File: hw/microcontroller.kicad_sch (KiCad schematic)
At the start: 65 parts, among them J201 68710814022, J202 FTSH-105-01-L-DV-K, SW201 Push button switch, U201 STM32H753VITx, U202 USB3343, Y201 26MHz, Y202 26MHz

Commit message: Now two CPLDs, new placement for better routing of clocks and symmetry for delay. Not routed yet but placement is "complete".
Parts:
- R221, R223, R224: footprint Resistor_SMD:R_0603_1608Metric -> Resistor_SMD:R_0402_1005Metric
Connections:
- net atten.12dB: now reaches U201.55 (PD8)
- net atten.6dB: now reaches U201.56 (PD9)
- net atten.3dB: now reaches U201.57 (PD10)
- net cpld1.NSS: now reaches U201.77 (PA15)
- net filter.BPFMid: now reaches U201.81 (PD0)
- net filter.BPFMid2: now reaches U201.82 (PD1)
- net filter.BPFHi: now reaches U201.83 (PD2)
- net filter.BPFLo1: now reaches U201.84 (PD3)
- net filter.HPF: now reaches U201.85 (PD4)
- net filter.BPFLo2: now reaches U201.86 (PD5)
- net atten.24dB: now reaches U201.88 (PD7)
- net cpld.MISO renamed cpld0.MISO
- net cpld.MOSI renamed cpld0.MOSI
- net cpld.NSS renamed cpld0.NSS
- net cpld.SCK renamed cpld0.SCK
- no-connect marks 37 -> 26
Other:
- note added: "SPI1=n/u SPI2=disp SPI3=cpld0/1 SPI4=osd0/1 SPI5=n/u SPI6=n/u"
- note removed: "SPI1=n/u SPI2=disp SPI3=cpld SPI4=osd0/1 SPI5=n/u SPI6=n/u"

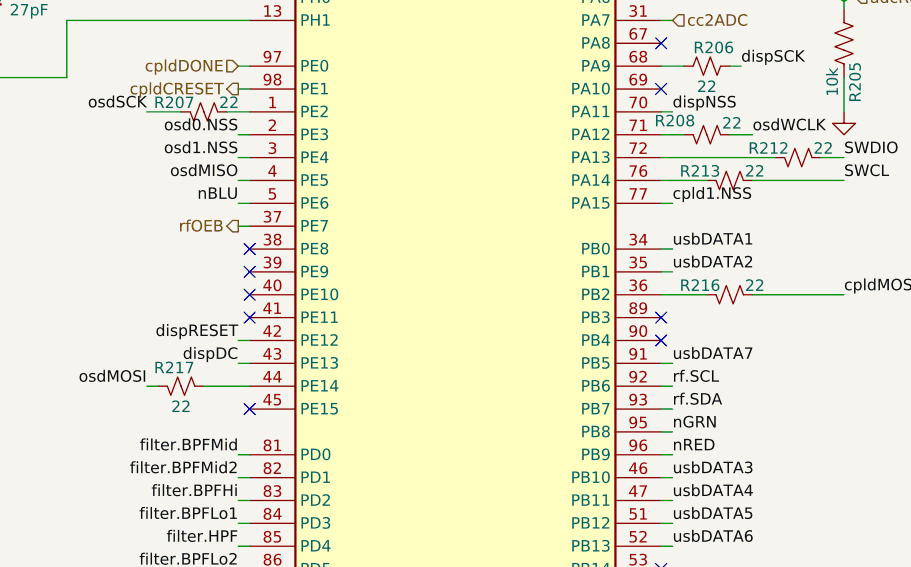
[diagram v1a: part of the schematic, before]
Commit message: PCB and schematic both pass DRC and all nets routed. Now for some desk checking...
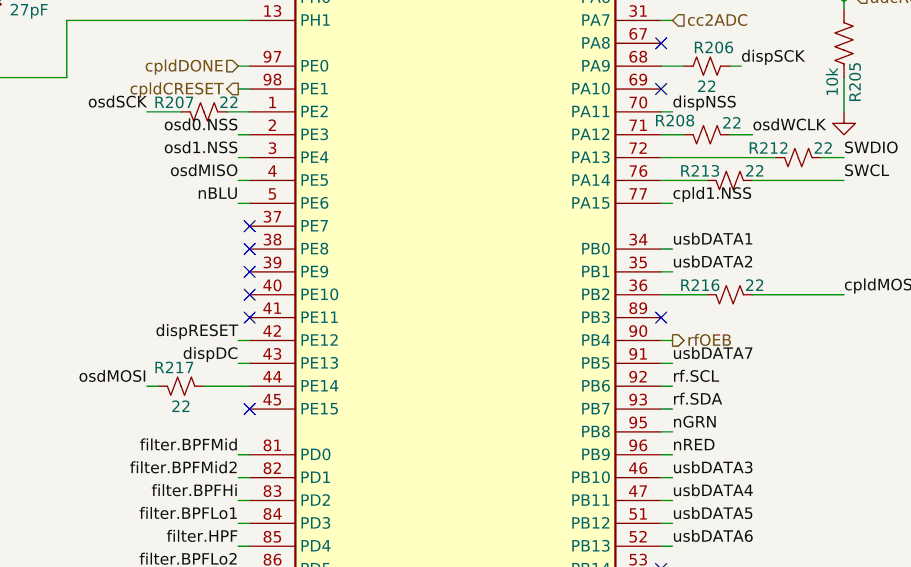
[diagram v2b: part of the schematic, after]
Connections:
- net rfOEB: now also U201.90 (PB4); no longer U201.37 (PE7)
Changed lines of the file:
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@@
 	)
 	(no_connect
-		(at 102.87 87.63)
-	)
-	(no_connect
 		(at 102.87 59.69)
 	)
@@
 	)
 	(no_connect
+		(at 57.15 74.93)
+	)
+	(no_connect
 		(at 102.87 151.13)
 	)
@@
 	(wire
 		(pts
-			(xy 55.88 74.93) (xy 57.15 74.93)
-		)
-		(stroke
-			(width 0)
-			(type default)
-		)
-	)
-	(wire
-		(pts
 			(xy 161.29 97.79) (xy 161.29 99.06)
 		)
@@
 	(wire
 		(pts
+			(xy 104.14 87.63) (xy 102.87 87.63)
+		)
+		(stroke
+			(width 0)
+			(type default)
+		)
+	)
+	(wire
+		(pts
 			(xy 134.62 133.35) (xy 134.62 134.62)
 		)
@@
 		)
 	)
+	(hierarchical_label "rfOEB"
+		(shape output)
+		(at 104.14 87.63 0)
+		(effects
+			(font
+				(size 1.27 1.27)
+			)
+			(justify left)
+		)
+	)
 	(hierarchical_label "rf{I2C}"
 		(shape bidirectional)
@@
 		)
 	)
-	(hierarchical_label "rfOEB"
-		(shape output)
-		(at 55.88 74.93 180)
-		(effects
-			(font
-				(size 1.27 1.27)
-			)
-			(justify right)
-		)
-	)

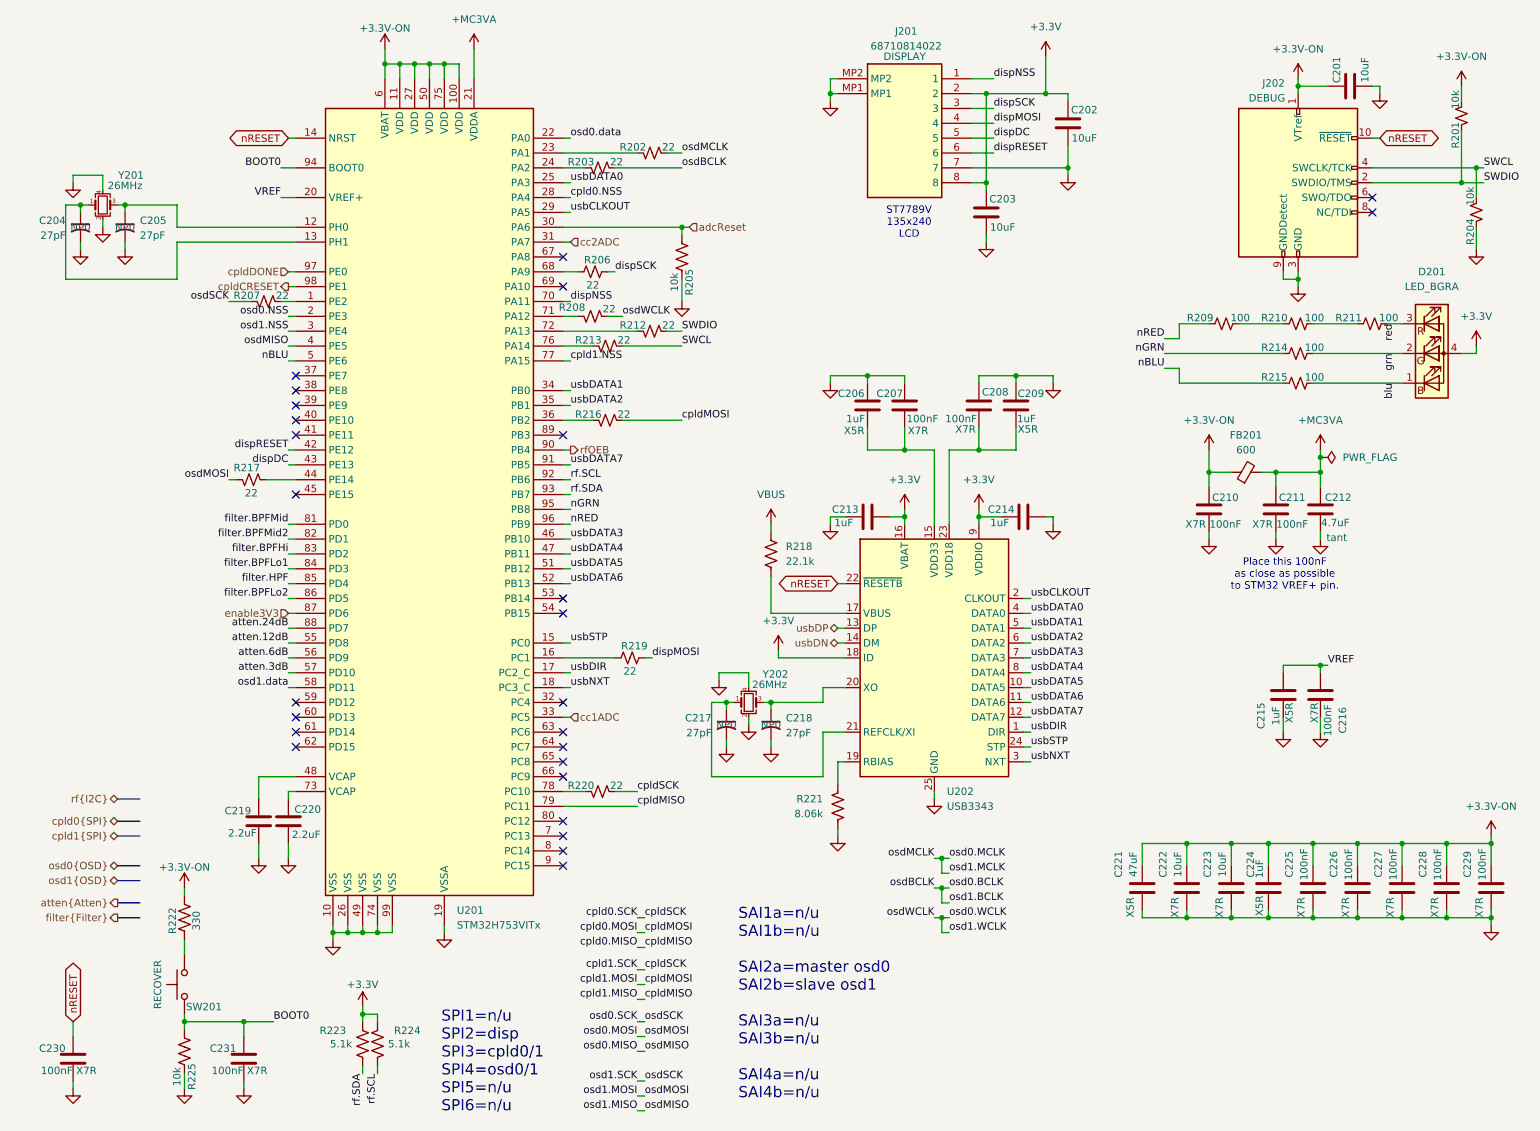
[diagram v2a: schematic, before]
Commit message: 3D rendering now. All DRCs pass on schematic and PCB. BOM scrubbed to coallesce parts. Still no part numbers for most.
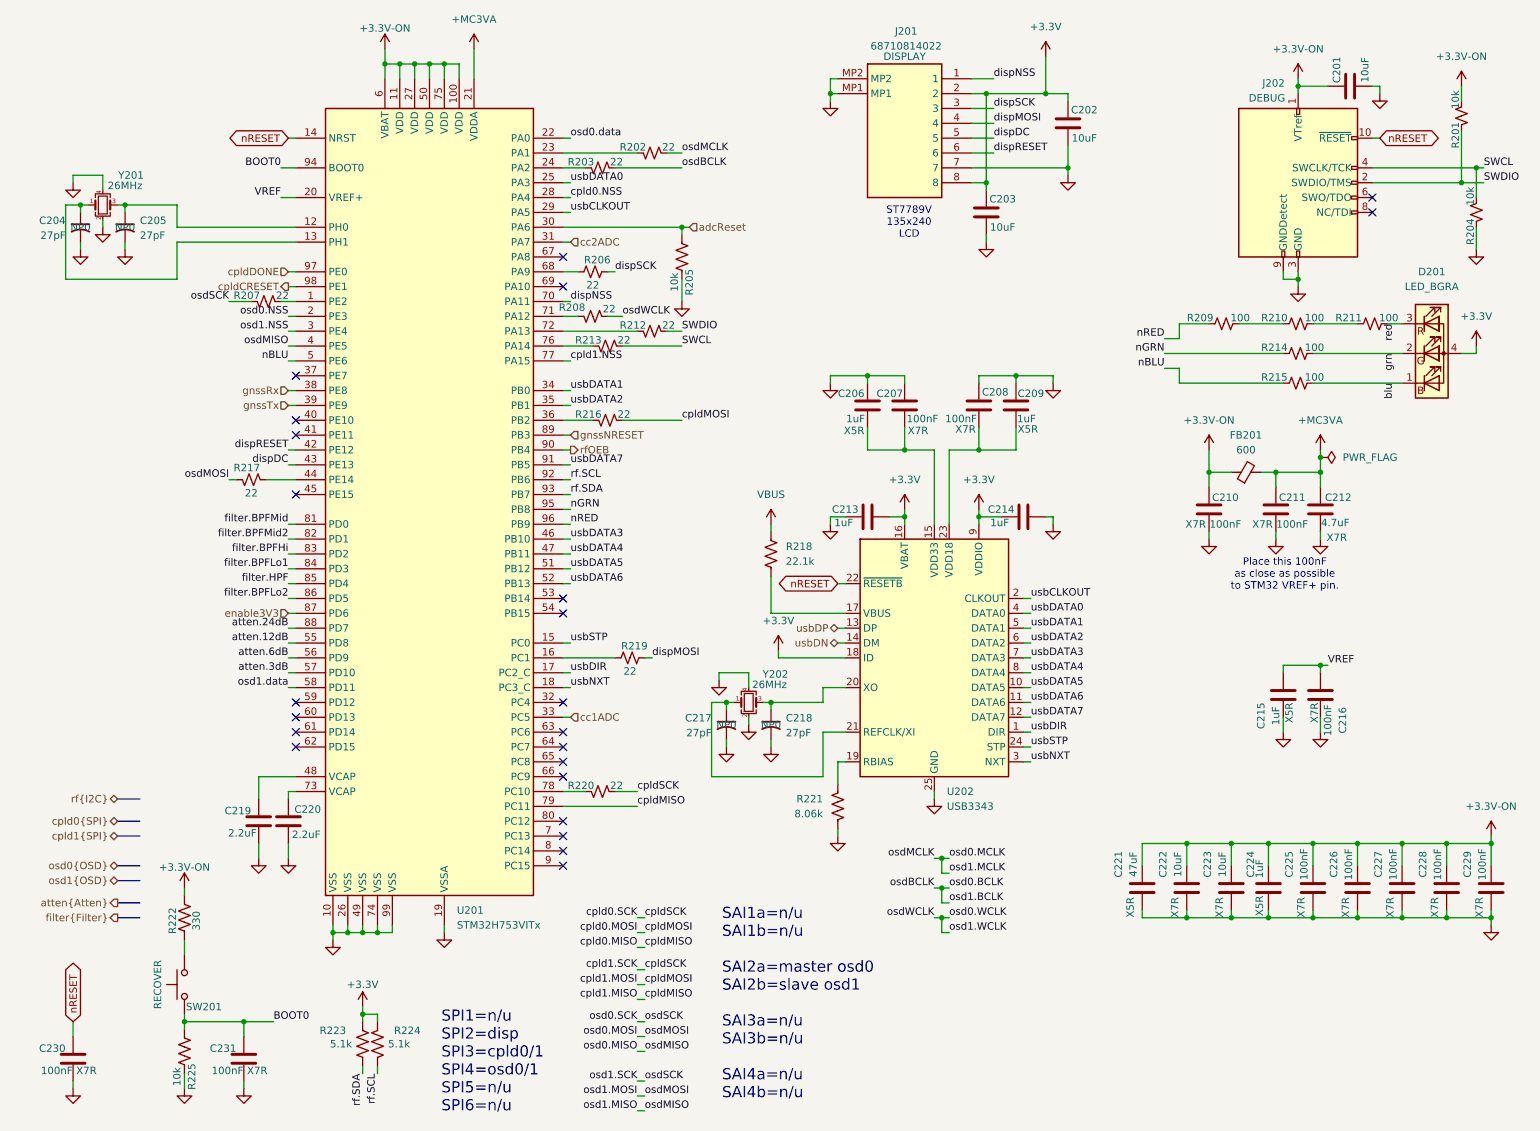
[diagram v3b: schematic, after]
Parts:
- C204, C205, C217, C218: working-voltage 50V -> 25V
- C212: footprint Capacitor_SMD:C_0805_2012Metric -> Capacitor_SMD:C_0402_1005Metric; cap-type tant -> X7R; working-voltage 10V -> 25V
- C219, C220: footprint Capacitor_SMD:C_0603_1608Metric -> Capacitor_SMD:C_0402_1005Metric; working-voltage 50V -> 25V
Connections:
- net gnssRx: now reaches U201.38 (PE8)
- net gnssTx: now reaches U201.39 (PE9)
- net gnssNRESET: now reaches U201.89 (PB3)
- no-connect marks 26 -> 23
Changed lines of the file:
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@@
 	(text "SAI1a=n/u\nSAI1b=n/u\n\nSAI2a=master osd0\nSAI2b=slave osd1\n\nSAI3a=n/u\nSAI3b=n/u\n\nSAI4a=n/u\nSAI4b=n/u\n"
 		(exclude_from_sim no)
-		(at 132.842 182.372 0)
+		(at 130.048 182.372 0)
 		(effects
 			(font
@@
 	)
 	(no_connect
-		(at 57.15 80.01)
-	)
-	(no_connect
 		(at 102.87 156.21)
 	)
@@
 	)
 	(no_connect
+		(at 57.15 74.93)
+	)
+	(no_connect
 		(at 102.87 59.69)
 	)
@@
 	)
 	(no_connect
-		(at 57.15 77.47)
-	)
-	(no_connect
 		(at 102.87 143.51)
 	)
 	(no_connect
-		(at 57.15 74.93)
-	)
-	(no_connect
 		(at 102.87 151.13)
 	)
@@
 	)
 	(no_connect
-		(at 102.87 85.09)
-	)
-	(no_connect
 		(at 102.87 54.61)
 	)
@@
 	(wire
 		(pts
+			(xy 55.88 80.01) (xy 57.15 80.01)
+		)
+		(stroke
+			(width 0)
+			(type default)
+		)
+	)
+	(wire
+		(pts
 			(xy 115.57 176.53) (xy 116.84 176.53)
 		)
@@
 	(wire
 		(pts
+			(xy 102.87 85.09) (xy 104.14 85.09)
+		)
+		(stroke
+			(width 0)
+			(type default)
+		)
+	)
+	(wire
+		(pts
 			(xy 139.7 123.19) (xy 151.13 123.19)
 		)
@@
 	(wire
 		(pts
+			(xy 55.88 77.47) (xy 57.15 77.47)
+		)
+		(stroke
+			(width 0)
+			(type default)
+		)
+	)
+	(wire
+		(pts
 			(xy 55.88 154.94) (xy 55.88 157.48)
 		)
@@
 		)
 	)
+	(hierarchical_label "gnssRx"
+		(shape input)
+		(at 55.88 77.47 180)
+		(effects
+			(font
+				(size 1.27 1.27)
+			)
+			(justify right)
+		)
+	)
 	(hierarchical_label "osd1{OSD}"
 		(shape bidirectional)
@@
 		)
 	)
+	(hierarchical_label "gnssTx"
+		(shape input)
+		(at 55.88 80.01 180)
+		(effects
+			(font
+				(size 1.27 1.27)
+			)
+			(justify right)
+		)
+	)
 	(hierarchical_label "adcReset"
 		(shape input)
@@
 		)
 	)
+	(hierarchical_label "gnssNRESET"
+		(shape input)
+		(at 104.14 85.09 0)
+		(effects
+			(font
+				(size 1.27 1.27)
+			)
+			(justify left)
+		)
+	)
 	(hierarchical_label "usbDN"
 		(shape bidirectional)
@@
 			)
 		)
-		(property "working-voltage" "50V"
+		(property "working-voltage" "25V"
 			(at 130.81 134.62 0)
 			(effects
@@
 			)
 		)
-		(property "working-voltage" "50V"
+		(property "working-voltage" "25V"
 			(at 138.43 134.62 0)
 			(effects
@@
 			)
 		)
-		(property "Footprint" "Capacitor_SMD:C_0603_1608Metric"
+		(property "Footprint" "Capacitor_SMD:C_0402_1005Metric"
 			(at 56.8452 154.94 0)
 			(effects
@@
 			)
 		)
-		(property "working-voltage" "50V"
+		(property "working-voltage" "25V"
 			(at 55.88 151.13 0)
 			(effects
@@
 			)
 		)
-		(property "Footprint" "Capacitor_SMD:C_0603_1608Metric"
+		(property "Footprint" "Capacitor_SMD:C_0402_1005Metric"
 			(at 49.8348 154.94 0)
 			(effects
@@
 			)
 		)
-		(property "working-voltage" "50V"
+		(property "working-voltage" "25V"
 			(at 50.8 151.13 0)
 			(effects
@@
 			)
 		)
-		(property "working-voltage" "50V"
+		(property "working-voltage" "25V"
 			(at 27.94 49.53 0)
 			(effects
@@
 			)
 		)
-		(property "Footprint" "Capacitor_SMD:C_0805_2012Metric"
+		(property "Footprint" "Capacitor_SMD:C_0402_1005Metric"
 			(at 233.3752 101.6 0)
 			(effects
@@
 			)
 		)
-		(property "cap-type" "tant"
+		(property "cap-type" "X7R"
 			(at 235.204 102.616 0)
 			(effects
@@
 			)
 		)
-		(property "working-voltage" "10V"
+		(property "working-voltage" "25V"
 			(at 232.41 97.79 0)
 			(effects
@@
 			)
 		)
-		(property "working-voltage" "50V"
+		(property "working-voltage" "25V"
 			(at 20.32 49.53 0)
 			(effects

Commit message: Not proud of the rats nest of controls for attenuator and filter, but now I have four filters (not five), all DRC pass, 3D renders properly, and I may tidy it up a bit later.
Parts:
- added C222, C223: 10uF, Capacitor_SMD:C_0402_1005Metric, symbol Device:C
- C201, C203: footprint Capacitor_SMD:C_0603_1608Metric -> Capacitor_SMD:C_0402_1005Metric; cap-type X7R -> X5R; working-voltage 25V -> 10V
- C202: footprint Capacitor_SMD:C_0603_1608Metric -> Capacitor_SMD:C_0402_1005Metric; JLCPCBpn C327087 -> (none); Manufacturer_Name Taoup Uidem -> (none); Manufacturer_Part_Number 81-GXT155R71E223KE1D -> (none); Mouser Part Number 963-MLAST168BB5106MT -> (none); cap-type X7R -> X5R; working-voltage 25V -> 10V
- C206, C209, C213, C214: JLCPCBpn C301928 -> (none); Manufacturer_Name Murata -> (none); Manufacturer_Part_Number GRM155R61E105KE11D -> (none); Mouser Part Number 81-GRM155R61E105KE1D -> (none)
- C221: value 47uF -> 10uF; footprint Capacitor_SMD:C_1206_3216Metric -> Capacitor_SMD:C_0402_1005Metric; LCSC_PN C403725 -> (none); MPN TCTAL1A107M8R-V1 -> (none); Manufacturer Kyocera AVX -> (none); Mouser_PN 755-TCTAL1A107M8R-V1 -> (none); working-voltage 25V -> 10V
- C224: renamed from C222; footprint Capacitor_SMD:C_0603_1608Metric -> Capacitor_SMD:C_0402_1005Metric; JLCPCBpn C327087 -> (none); Manufacturer_Name Taoup Uidem -> (none); Manufacturer_Part_Number 81-GXT155R71E223KE1D -> (none); Mouser Part Number 963-MLAST168BB5106MT -> (none); cap-type X7R -> X5R; working-voltage 25V -> 10V
- C225: renamed from C223; footprint Capacitor_SMD:C_0603_1608Metric -> Capacitor_SMD:C_0402_1005Metric; JLCPCBpn C327087 -> (none); Manufacturer_Name Taoup Uidem -> (none); Manufacturer_Part_Number 81-GXT155R71E223KE1D -> (none); Mouser Part Number 963-MLAST168BB5106MT -> (none); cap-type X7R -> X5R; working-voltage 25V -> 10V
- renumbered C224 to C226, C225 to C227, C226 to C228, C227 to C229, C228 to C230, C229 to C231, C230 to C232, C231 to C233
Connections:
- net filter.BPFMid is gone; now on net filter.BPFLo2: U201.81 (PD0)
- net filter.BPFMid2 is gone; now on net filter.BPFLo1: U201.82 (PD1)
- net +3.3V-ON: now also C222.1, C223.1
- net GND: now also C222.2, C223.2
- net atten.24dB: now also U201.56 (PD9); no longer U201.88 (PD7)
- net atten.6dB: now also U201.88 (PD7); no longer U201.56 (PD9)
- net filter.BPFHi: now also U201.84 (PD3); no longer U201.83 (PD2)
- net filter.BPFLo1: no longer U201.84 (PD3)
- net filter.BPFLo2: no longer U201.86 (PD5)
- net filter.HPF: now also U201.83 (PD2); no longer U201.85 (PD4)
- new net filter.BPFHi1: U201.86 (PD5)
- new net filter.BPFHi2: U201.85 (PD4)

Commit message: Set up for DVT2 PCBA build at JLCPCB
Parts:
- C201, C203: MPN 81-GXT155R71E223KE1D -> (none)
- C205, C217, C218: JLCPCBpn C107045 -> (none)
- C207, C208, C210, C211, C231: MPN C0805F104K1RACAUTO -> (none)
- C212: MPN 298D475X9010M2T -> (none)
- C215, C226: MPN GRM155R61E105KE11D -> (none)
- Y201, Y202: MFG (none) -> EATON; Manufacturer_Name EATON -> (none); Manufacturer_Part_Number E2X260181G01 -> (none)
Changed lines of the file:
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@@
 			)
 		)
-		(property "MPN" "C0805F104K1RACAUTO"
+		(property "MPN" ""
 			(at 0 0 0)
 			(effects
@@
 			)
 		)
+		(property "cap-type" ""
+			(at 251.46 71.12 0)
+			(effects
+				(font
+					(size 1.27 1.27)
+				)
+			)
+		)
+		(property "r-power" ""
+			(at 251.46 71.12 0)
+			(effects
+				(font
+					(size 1.27 1.27)
+				)
+			)
+		)
+		(property "label" ""
+			(at 251.46 71.12 0)
+			(effects
+				(font
+					(size 1.27 1.27)
+				)
+			)
+		)
 		(pin "3"
 		)
@@
 			)
 		)
-		(property "JLCPCBpn" "C107045"
+		(property "JLCPCBpn" ""
 			(at 130.81 134.62 0)
 			(effects
@@
 			)
 		)
-		(property "MPN" "C0805F104K1RACAUTO"
+		(property "MPN" ""
 			(at 0 0 0)
 			(effects
@@
 			)
 		)
-		(property "JLCPCBpn" "C107045"
+		(property "JLCPCBpn" ""
 			(at 138.43 134.62 0)
 			(effects
@@
 			)
 		)
-		(property "MPN" "GRM155R61E105KE11D"
+		(property "MPN" ""
 			(at 0 0 0)
 			(effects
@@
 			)
 		)
-		(property "JLCPCBpn" "C107045"
+		(property "JLCPCBpn" ""
 			(at 27.94 49.53 0)
 			(effects
@@
 			)
 		)
-		(property "MPN" "C0805F104K1RACAUTO"
+		(property "MPN" ""
 			(at 0 0 0)
 			(effects
@@
 			)
 		)
-		(property "MPN" "GRM155R61E105KE11D"
+		(property "MPN" ""
 			(at 0 0 0)
 			(effects
@@
 			)
 		)
-		(property "Manufacturer_Name" "EATON"
+		(property "Manufacturer_Name" ""
 			(at 145.415 139.065 90)
 			(effects
@@
 			)
 		)
-		(property "Manufacturer_Part_Number" "E2X260181G01"
+		(property "Manufacturer_Part_Number" ""
 			(at 148.59 142.875 90)
 			(effects
@@
 			)
 		)
+		(property "MFG" "EATON"
+			(at 134.62 130.81 0)
+			(effects
+				(font
+					(size 1.27 1.27)
+				)
+				(hide yes)
+			)
+		)
 		(pin "3"
 		)
@@
 			)
 		)
-		(property "MPN" "81-GXT155R71E223KE1D"
+		(property "MPN" ""
 			(at 0 0 0)
 			(effects
@@
 			)
 		)
-		(property "MPN" "C0805F104K1RACAUTO"
+		(property "MPN" ""
 			(at 0 0 0)
 			(effects
@@
 			)
 		)
-		(property "MPN" "298D475X9010M2T"
+		(property "MPN" ""
 			(at 0 0 0)
 			(effects
@@
 			)
 		)
-		(property "MPN" "C0805F104K1RACAUTO"
+		(property "MPN" ""
 			(at 0 0 0)
 			(effects
@@
 			)
 		)
-		(property "Manufacturer_Name" "EATON"
+		(property "Manufacturer_Name" ""
 			(at 34.925 53.975 90)
 			(effects
@@
 			)
 		)
-		(property "Manufacturer_Part_Number" "E2X260181G01"
+		(property "Manufacturer_Part_Number" ""
 			(at 38.1 57.785 90)
 			(effects
@@
 			)
 		)
+		(property "MFG" "EATON"
+			(at 24.13 45.72 0)
+			(effects
+				(font
+					(size 1.27 1.27)
+				)
+				(hide yes)
+			)
+		)
 		(pin "3"
 		)
@@
 			)
 		)
-		(property "MPN" "81-GXT155R71E223KE1D"
+		(property "MPN" ""
 			(at 0 0 0)
 			(effects

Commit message: DVT2 try #2. This is the one from which I ordered PCBs (bare only) from JLCPCB
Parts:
- R202, R203: JLCPCBpn (none) -> C4258780
- U201: value STM32H753VITx -> STM32H743VIT6; LCSC_PN C730206 -> C114409; MPN (none) -> STM32H743VIT6; Manufacturer (none) -> ST Micro
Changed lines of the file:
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@@
 			)
 		)
+		(property "JLCPCBpn" "C4258780"
+			(at 118.11 36.83 90)
+			(effects
+				(font
+					(size 1.27 1.27)
+				)
+				(hide yes)
+			)
+		)
 		(pin "1"
 		)
@@
 			)
 		)
+		(property "JLCPCBpn" "C4258780"
+			(at 109.22 39.37 90)
+			(effects
+				(font
+					(size 1.27 1.27)
+				)
+				(hide yes)
+			)
+		)
 		(pin "1"
 		)
@@
 			)
 		)
-		(property "Value" "STM32H753VITx"
+		(property "Value" "STM32H743VIT6"
 			(at 84.6933 168.91 0)
 			(effects
@@
 			)
 		)
-		(property "Datasheet" "https://www.st.com/resource/en/datasheet/stm32h753vi.pdf"
+		(property "Datasheet" "https://www.st.com/resource/en/datasheet/stm32h743vi.pdf"
 			(at 80.01 97.79 0)
 			(effects
@@
 			)
 		)
-		(property "Manufacturer" ""
+		(property "Manufacturer" "ST Micro"
 			(at 0 0 0)
 			(effects
@@
 			)
 		)
-		(property "MPN" ""
+		(property "MPN" "STM32H743VIT6"
 			(at 0 0 0)
 			(effects
@@
 			)
 		)
-		(property "LCSC_PN" "C730206"
+		(property "LCSC_PN" "C114409"
 			(at 0 0 0)
 			(effects

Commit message: Cleaned up some vias, some traces, resubmitted to JLCPCB as DVT2-20260812.
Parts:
- added R222, R223, R224, R225: 10k, Resistor_SMD:R_0402_1005Metric, symbol Device:R_US
- R221: value 8.06k -> 1k; LCSC_PN C863964 -> C136974
- renumbered R222 to R226, R223 to R227, R224 to R228, R225 to R229
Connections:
- net GND: now also R223.2, R225.2; no longer R221.2
- net at R221.1, U202.19 (RBIAS): now also R222.1
- new net: R221.2, R223.1
- new net: R222.2, R224.1
- new net: R224.2, R225.1
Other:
- note added: "This baroque mess is 8048.8 ohms without adding a singleton."
